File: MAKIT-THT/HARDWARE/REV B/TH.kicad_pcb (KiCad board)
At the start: 2 copper layers, 68.6 x 53.1 mm, 29 parts, among them P1 USB_A, P2 BARREL_JACK, P3 CONN_01X08, P4 CONN_01X06, P5 CONN_01X10, P6 CONN_01X08, P7 ICSP, SW1 Push_SW, U1 LM7805CT, U2 MCP2221A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

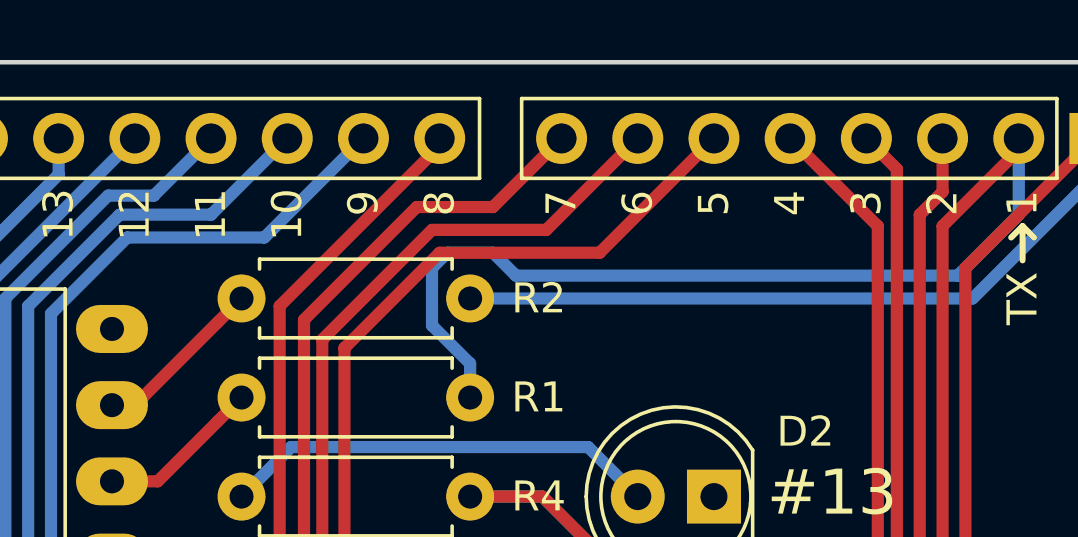
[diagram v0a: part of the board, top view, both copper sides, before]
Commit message: replaced A7 for SIM 800L
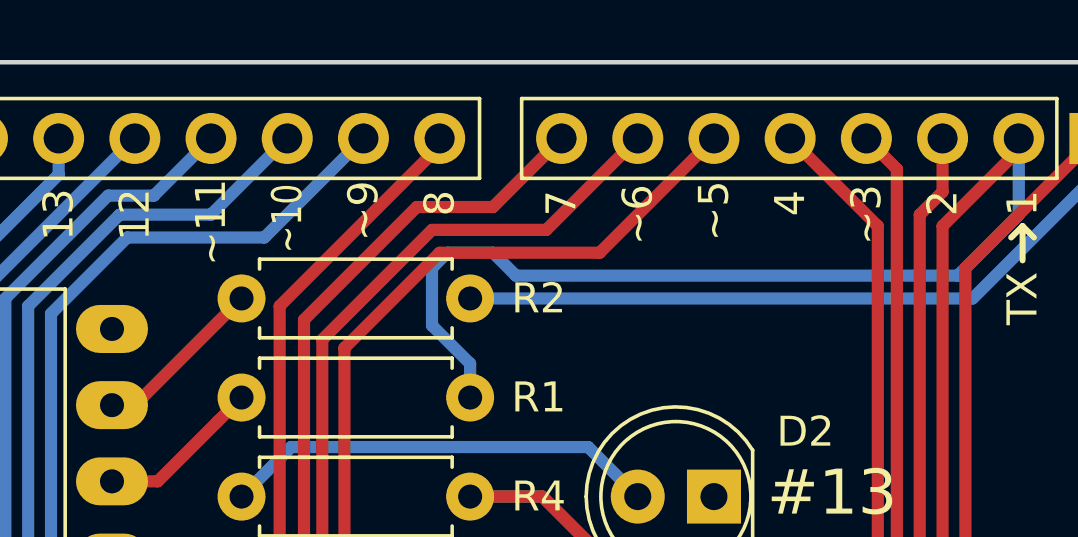
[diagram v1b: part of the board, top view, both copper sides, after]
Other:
- board text added: "~~10"
- board text added: "~~11"
- board text added: "~~3"
- board text added: "~~5"
- board text added: "~~6"
- board text added: "~~9"
- board text removed: "10"
- board text removed: "11"
- board text removed: "3"
- board text removed: "5"
- board text removed: "6"
- board text removed: "9"
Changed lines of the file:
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@@
     (links 88)
     (no_connects 0)
-    (area 106.604999 26.340999 175.335001 79.577001)
+    (area 101.499999 23.919466 203.300001 127.100001)
     (thickness 1.6)
     (drawings 61)
@@
       (drillshape 0)
       (scaleselection 1)
-      (outputdirectory "TH PANEL"))
+      (outputdirectory MAKIT_THT_REVB_GERBER))
   )
   (net 0 "")
@@
     (effects (font (size 1 1) (thickness 0.15)))
   )
-  (gr_text 3 (at 162.56 31.115 90) (layer F.SilkS)
+  (gr_text ~~3 (at 162.56 31.496 90) (layer F.SilkS)
     (effects (font (size 1 1) (thickness 0.15)))
   )
@@
     (effects (font (size 1 1) (thickness 0.15)))
   )
-  (gr_text 5 (at 157.48 31.115 90) (layer F.SilkS)
+  (gr_text ~~5 (at 157.48 31.369 90) (layer F.SilkS)
     (effects (font (size 1 1) (thickness 0.15)))
   )
-  (gr_text 6 (at 154.94 31.115 90) (layer F.SilkS)
+  (gr_text ~~6 (at 154.94 31.496 90) (layer F.SilkS)
     (effects (font (size 1 1) (thickness 0.15)))
   )
@@
     (effects (font (size 1 1) (thickness 0.15)))
   )
-  (gr_text 9 (at 145.796 31.115 90) (layer F.SilkS)
+  (gr_text ~~9 (at 145.796 31.369 90) (layer F.SilkS)
     (effects (font (size 1 1) (thickness 0.15)))
   )
-  (gr_text 10 (at 143.256 31.496 90) (layer F.SilkS)
+  (gr_text ~~10 (at 143.256 31.623 90) (layer F.SilkS)
+    (effects (font (size 1 0.8) (thickness 0.15)))
+  )
+  (gr_text ~~11 (at 140.716 31.75 90) (layer F.SilkS)
     (effects (font (size 1 1) (thickness 0.15)))
   )
-  (gr_text 11 (at 140.716 31.496 90) (layer F.SilkS)
-    (effects (font (size 1 1) (thickness 0.15)))
-  )
